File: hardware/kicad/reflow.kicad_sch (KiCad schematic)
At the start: 0 parts

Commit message: hardware: place all schematic components
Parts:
- added A1: ESP32-DevKitV1, reflow:ESP32_DevKitV1_2x15_P2.54_W22.86, symbol reflow:ESP32_DevKitV1
- added C1: 100uF, Capacitor_THT:CP_Radial_D8.0mm_P3.50mm, symbol Device:C
- added C2: 1000uF, Capacitor_THT:CP_Radial_D10.0mm_P5.00mm, symbol Device:C
- added C3, C5, C6, C7, C8: 100nF, Capacitor_THT:C_Disc_D5.0mm_W2.5mm_P2.50mm, symbol Device:C
- added C4: 10uF, Capacitor_THT:CP_Radial_D5.0mm_P2.50mm, symbol Device:C
- added D1: STATUS, LED_THT:LED_D5.0mm, symbol Device:LED
- added D2: 1N5817, Diode_THT:D_DO-41_SOD81_P10.16mm_Horizontal, symbol Device:D_Schottky
- added D3: SMBJ26A, Diode_THT:D_DO-201AD_P15.24mm_Horizontal, symbol Device:D_TVS
- added F1: 15A, Fuse:Fuseholder_Cylinder-5x20mm_Schurter_FAB_0031.8201_Horizontal_Closed, symbol Device:Fuse
- added J1: 24V_IN, TerminalBlock:TerminalBlock_bornier-2_P5.08mm, symbol TerminalBlock:TerminalBlock_bornier-2_P5.08mm
- added J2: HEATER, TerminalBlock:TerminalBlock_bornier-2_P5.08mm, symbol TerminalBlock:TerminalBlock_bornier-2_P5.08mm
- added J3: MAX31855, reflow:Header_1x05_P2.54, symbol reflow:MAX31855_Module
- added J4: OLED, reflow:Header_1x04_P2.54, symbol reflow:OLED_SSD1306_I2C
- added L1: 100uH, Inductor_THT:L_Toroid_Vertical_L20.0mm_D7.0mm_P10.16mm, symbol Device:L
- added Q1: IRFS4710, energy_system:TO-220-3_Vertical_LaserPads_GDS, symbol Transistor_FET:Q_NMOS_GDS
- added Q2, Q3: BS170, Package_TO_SOT_THT:TO-92_Inline, symbol Transistor_FET:Q_NMOS_GDS
- added R1, R2: 1k, Resistor_THT:R_Axial_DIN0207_L6.3mm_D2.5mm_P7.62mm_Horizontal, symbol Device:R
- added R10, R11, R12, R3, R5, R9: 10k, Resistor_THT:R_Axial_DIN0207_L6.3mm_D2.5mm_P7.62mm_Horizontal, symbol Device:R
- added R4: 100, Resistor_THT:R_Axial_DIN0207_L6.3mm_D2.5mm_P7.62mm_Horizontal, symbol Device:R
- added R6: 330, Resistor_THT:R_Axial_DIN0207_L6.3mm_D2.5mm_P7.62mm_Horizontal, symbol Device:R
- added R7, R8: 4.7k, Resistor_THT:R_Axial_DIN0207_L6.3mm_D2.5mm_P7.62mm_Horizontal, symbol Device:R
- added SW1: ENC, Rotary_Encoder:RotaryEncoder_Alps_EC11E-Switch, symbol Device:RotaryEncoder_Switch
- added SW2: START, Button_Switch_THT:SW_PUSH_6mm, symbol Switch:SW_Push
- added U2: LM2576-5.0, energy_system:TO-220-3_Vertical_LaserPads, symbol Regulator_Switching:LM2576T-5
- added U3: LM7812, energy_system:TO-220-3_Vertical_LaserPads, symbol Regulator_Linear:LM7812_TO220

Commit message: hardware: fix MOSFET lib_id to Device:Q_NMOS_GDS; add U2 footprint TODO
Change Q1/Q2/Q3 lib_id from Transistor_FET:Q_NMOS_GDS to Device:Q_NMOS_GDS
(standard KiCad 10 location) in both the PIN_IDS map and COMPONENTS list.
Add inline TODO on U2 noting the 5-pin LM2576 needs a TO-220-5 laser-pad
footprint variant before board layout.

Regenerated reflow.kicad_sch: 37 components, placement check MISSING [],
kicad-cli export exits 0 with no unresolved-symbol warnings,
Transistor_FET:Q_NMOS_GDS count=0, Device:Q_NMOS_GDS count=3.
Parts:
- removed Q1: IRFS4710, energy_system:TO-220-3_Vertical_LaserPads_GDS, symbol Transistor_FET:Q_NMOS_GDS
- removed Q2, Q3: BS170, Package_TO_SOT_THT:TO-92_Inline, symbol Transistor_FET:Q_NMOS_GDS
- added Q1: IRFS4710, energy_system:TO-220-3_Vertical_LaserPads_GDS, symbol Device:Q_NMOS_GDS
- added Q2, Q3: BS170, Package_TO_SOT_THT:TO-92_Inline, symbol Device:Q_NMOS_GDS
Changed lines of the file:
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@@
 	)
 	(symbol
-		(lib_id "Transistor_FET:Q_NMOS_GDS")
+		(lib_id "Device:Q_NMOS_GDS")
 		(at 330 220 0)
 		(unit 1)
@@
 	)
 	(symbol
-		(lib_id "Transistor_FET:Q_NMOS_GDS")
+		(lib_id "Device:Q_NMOS_GDS")
 		(at 270 230 0)
 		(unit 1)
@@
 	)
 	(symbol
-		(lib_id "Transistor_FET:Q_NMOS_GDS")
+		(lib_id "Device:Q_NMOS_GDS")
 		(at 300 230 0)
 		(unit 1)

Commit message: hardware: wire 24V input protection, LM2576 5V, LM7812 12V rails
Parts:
- removed J1: 24V_IN, TerminalBlock:TerminalBlock_bornier-2_P5.08mm, symbol TerminalBlock:TerminalBlock_bornier-2_P5.08mm
- removed J2: HEATER, TerminalBlock:TerminalBlock_bornier-2_P5.08mm, symbol TerminalBlock:TerminalBlock_bornier-2_P5.08mm
- removed Q1: IRFS4710, energy_system:TO-220-3_Vertical_LaserPads_GDS, symbol Device:Q_NMOS_GDS
- removed Q2, Q3: BS170, Package_TO_SOT_THT:TO-92_Inline, symbol Device:Q_NMOS_GDS
- added J1: 24V_IN, TerminalBlock:TerminalBlock_bornier-2_P5.08mm, symbol Connector:Screw_Terminal_01x02
- added J2: HEATER, TerminalBlock:TerminalBlock_bornier-2_P5.08mm, symbol Connector:Screw_Terminal_01x02
- added Q1: IRFS4710, energy_system:TO-220-3_Vertical_LaserPads_GDS, symbol Transistor_FET:Q_NMOS_GDS
- added Q2, Q3: BS170, Package_TO_SOT_THT:TO-92_Inline, symbol Transistor_FET:Q_NMOS_GDS
- C3: value 100nF -> 330nF
- C4: value 10uF -> 100nF; footprint Capacitor_THT:CP_Radial_D5.0mm_P2.50mm -> Capacitor_THT:C_Disc_D5.0mm_W2.5mm_P2.50mm
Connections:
- new net: F1.1, J1.1 (Pin_1)
- new net +12V: C4.1, U3.3 (VO)
- new net +24V: C1.1, C3.1, D3.1 (A1), F1.2, J2.1 (Pin_1), U2.1 (VIN), U3.1 (VI)
- new net +5V: C2.1, L1.2, U2.4 (FB)
- new net GND: C1.2, C2.2, C3.2, C4.2, D2.2 (A), D3.2 (A2), J1.2 (Pin_2), U2.3 (GND), U2.5 (~{ON}/OFF), U3.2 (GND)
- new net SW_OUT: D2.1 (K), L1.1, U2.2 (OUT)

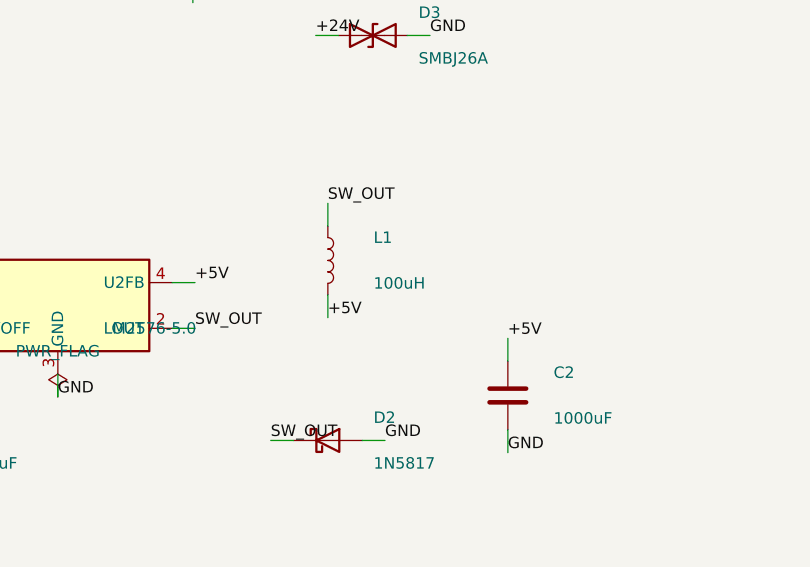
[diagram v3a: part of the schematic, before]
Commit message: hw(buck): swap L1 to 120uH 1A to clear peak-current margin
The 100uH/0.66A shop inductor was below the calculated LM2576 peak
inductor current (~0.82-0.88A at 0.5A load). Replace with the DTU
shop 120uH/1A part: 1A rating exceeds the 0.82A peak with ~20% margin
and reduces ripple from ~0.76A(pp) to ~0.63A(pp).

Update electrical-calcs.md with recomputed ripple (0.63A pp) and peak
(0.82A) for L=120uH, and confirm 1A rating provides adequate margin.
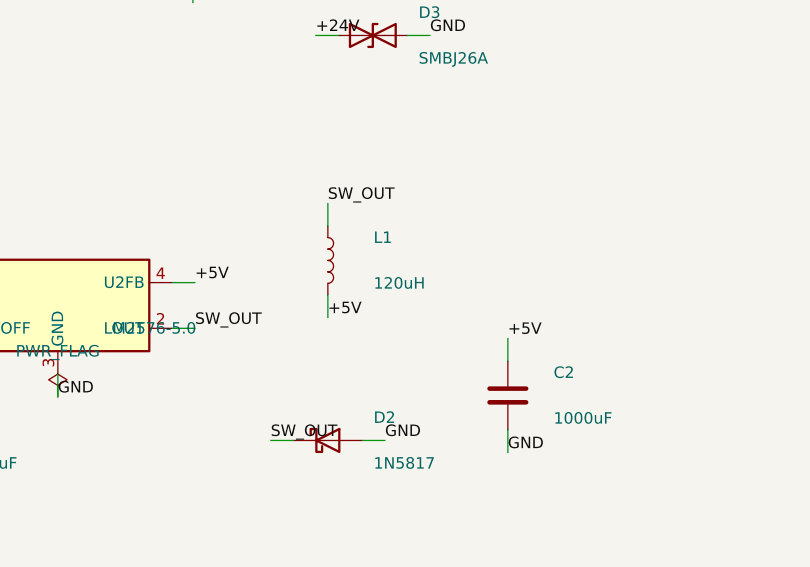
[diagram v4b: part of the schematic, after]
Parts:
- L1: value 100uH -> 120uH
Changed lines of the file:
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@@
 			)
 		)
-		(property "Value" "100uH"
+		(property "Value" "120uH"
 			(at 75.08 77.54 0)
 			(effects

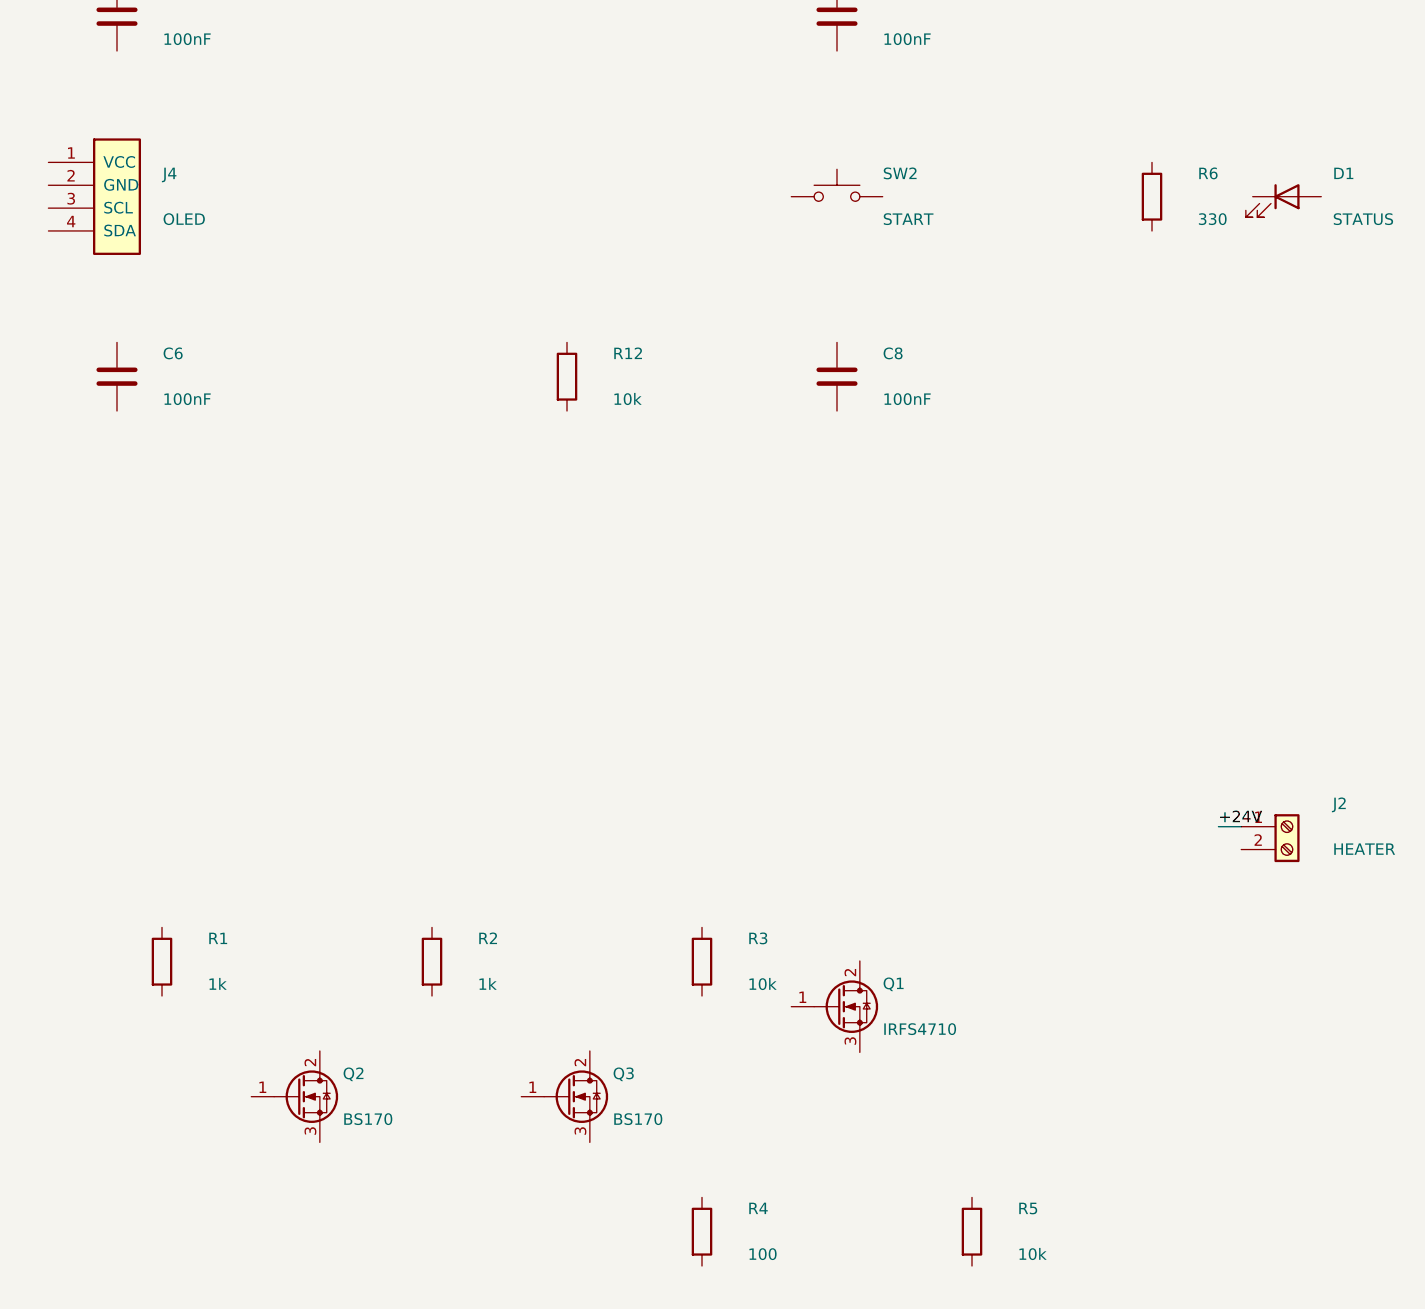
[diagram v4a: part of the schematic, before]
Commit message: hardware: wire IRFS4710 power stage with boot-safe two-stage gate drive
Add NETS_POWERSTAGE wiring pass: two-stage non-inverting BS170 level
shifter (Q2/Q3) driving the IRFS4710 (Q1) low-side heater switch.

- R1 100k Q2.G->GND pulldown, R2 1k HEATER_PWM->Q2.G series
- R3 10k GD_NODE1->+12V pull-up, R4 10k GATE_MAIN->+12V pull-up
- R5 100R series gate resistor, R6 10k Q1.G->GND gate-source pulldown
- HEATER_RET = J2.2 = Q1.D; D4 SMBJ33A TVS clamps drain transients
- Reassign R6 to the gate pulldown (per brief); status-LED resistor -> R13

Boot-safe: floating/low GPIO -> Q2 off -> GD_NODE1=+12V -> Q3 on ->
GATE_MAIN=0V -> Q1 off (heater inherently OFF). Add check_gate_boot_safe.py
asserting the non-inverting pattern and rejecting the single-inverting one.
Power-stage ERC clean; remaining ERC errors are Task-6 refs only.
Append Q1 conduction loss, gate-switching, Vgs and TVS calcs.
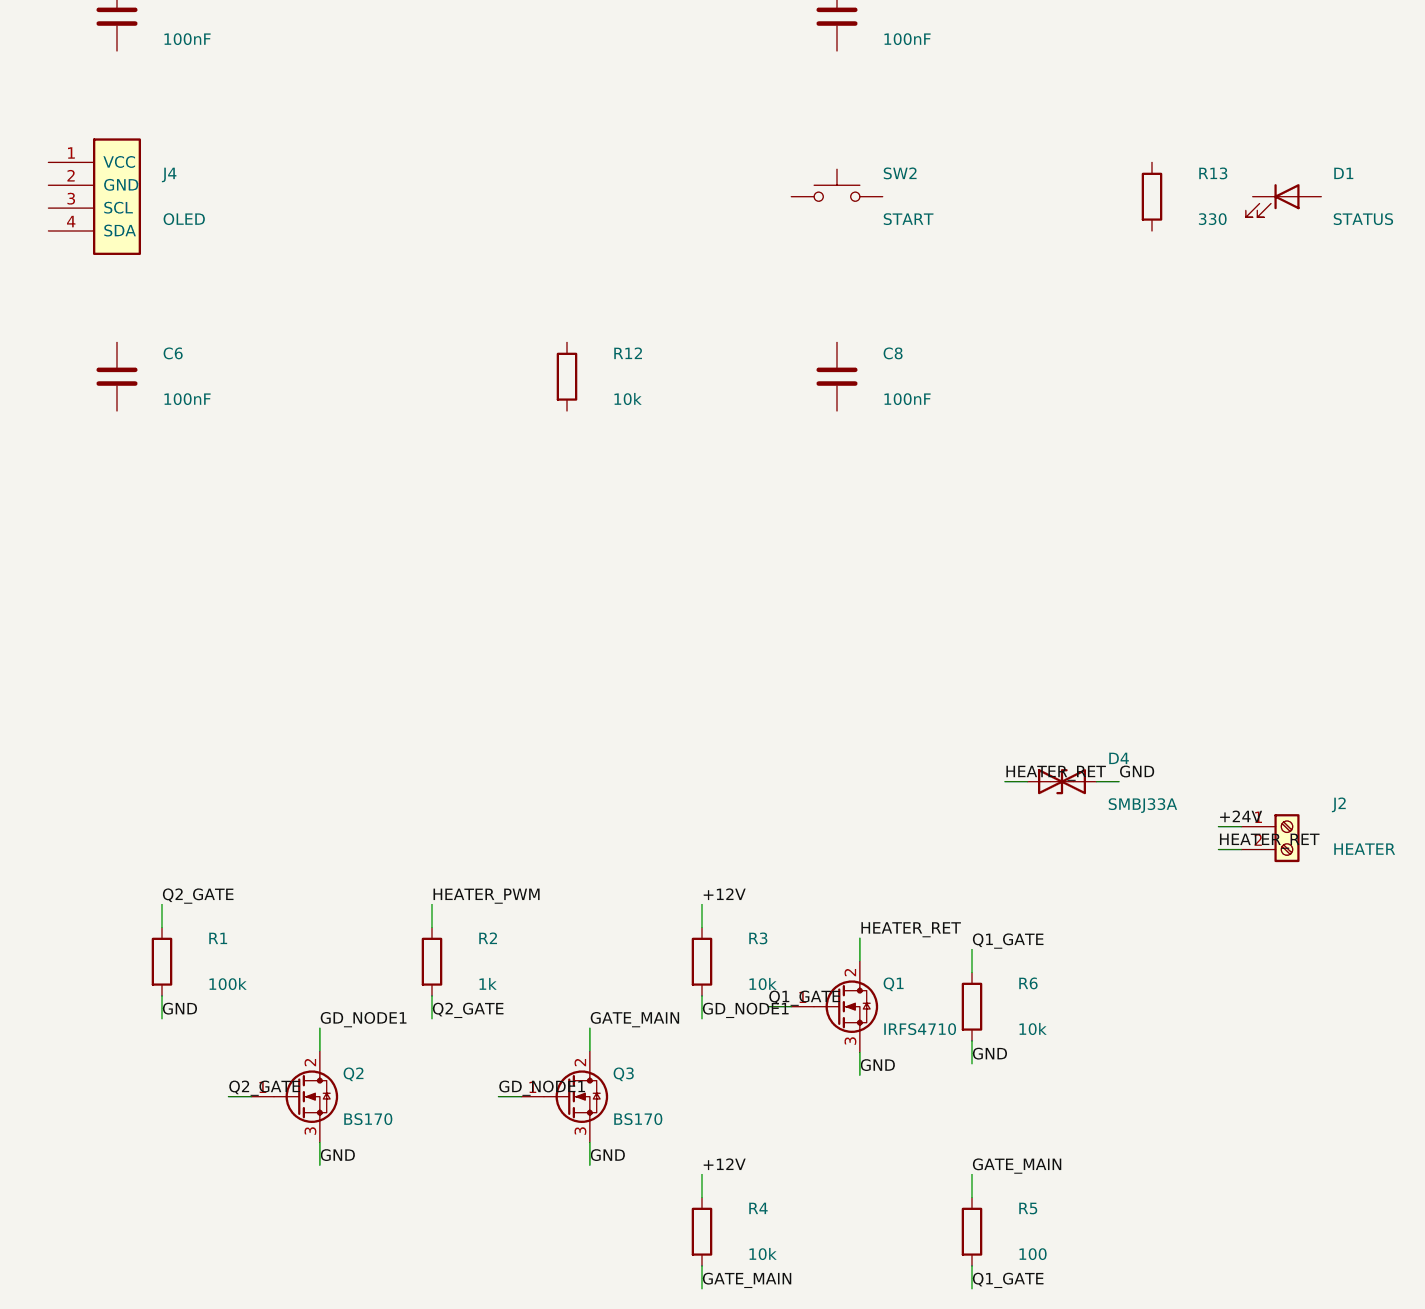
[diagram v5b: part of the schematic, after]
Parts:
- added D4: SMBJ33A, Diode_THT:D_DO-201AD_P15.24mm_Horizontal, symbol Device:D_TVS
- added R13: 330, Resistor_THT:R_Axial_DIN0207_L6.3mm_D2.5mm_P7.62mm_Horizontal, symbol Device:R
- R1: value 1k -> 100k
- R4: value 100 -> 10k
- R5: value 10k -> 100
- R6: value 330 -> 10k
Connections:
- net +12V: now also R3.1, R4.1
- net GND: now also Q1.3 (S), Q2.3 (S), Q3.3 (S), R1.2, R6.2, D4.2 (A2)
- net GD_NODE1: now reaches R3.2
- net GD_NODE1: now also Q2.2 (D), Q3.1 (G)
- net Q2_GATE: now reaches R1.1
- net Q2_GATE: now also Q2.1 (G), R2.2
- net HEATER_PWM: now reaches R2.1
- net Q1_GATE: now reaches R6.1
- net Q1_GATE: now also Q1.1 (G), R5.2
- net HEATER_RET: now reaches Q1.2 (D)
- net HEATER_RET: now also J2.2 (Pin_2), D4.1 (A1)
- net GATE_MAIN: now reaches R4.2
- net GATE_MAIN: now also Q3.2 (D), R5.1

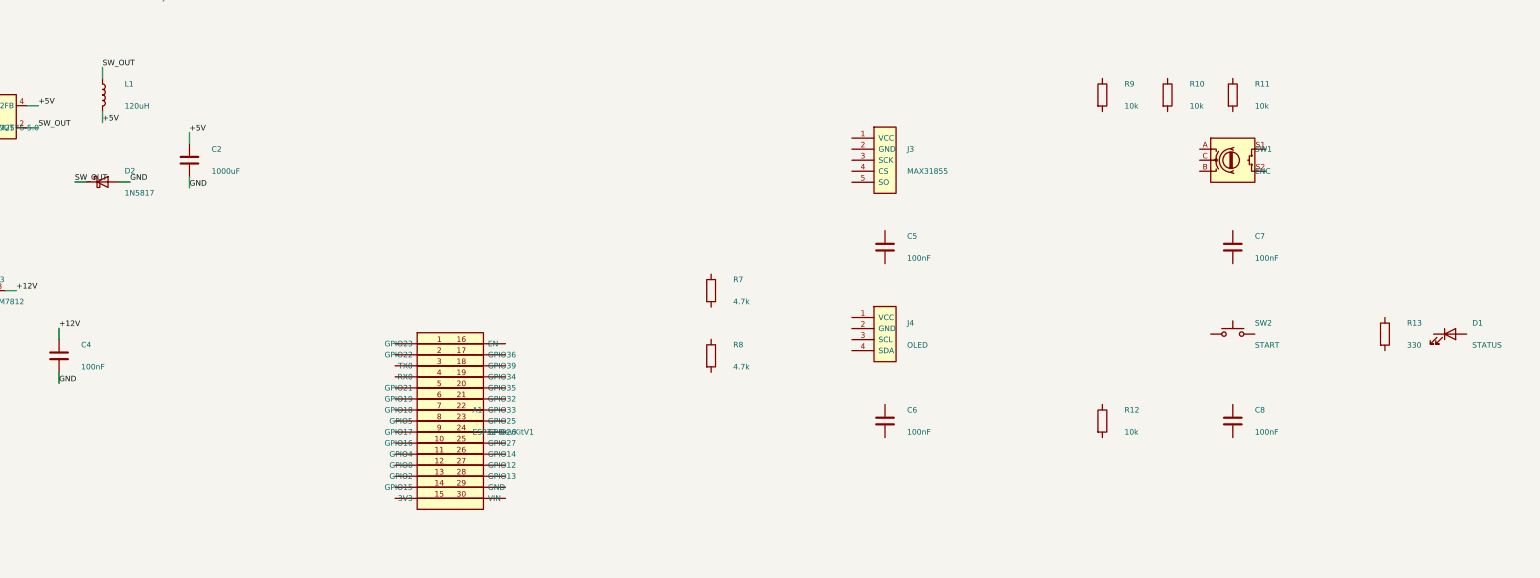
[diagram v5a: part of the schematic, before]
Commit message: hardware: wire ESP32, MAX31855 SPI, OLED I2C, encoder, button, status LED
Add NETS_CTRL pass realising every pinmap GPIO on the ESP32 pins plus the
J3/J4/SW1/SW2/D1 peripherals and their decoupling/debounce caps. Remove the
orphaned R7-R12 placeholders (encoder/button use internal pull-ups; OLED has
its own I2C pull-ups) so the resistor set is R1-R6 + R13. Add +3V3 and +5V
PWR_FLAGs to give those rails an ERC driver. net_contract now passes; the
controller section has no unconnected/undriven ERC errors.
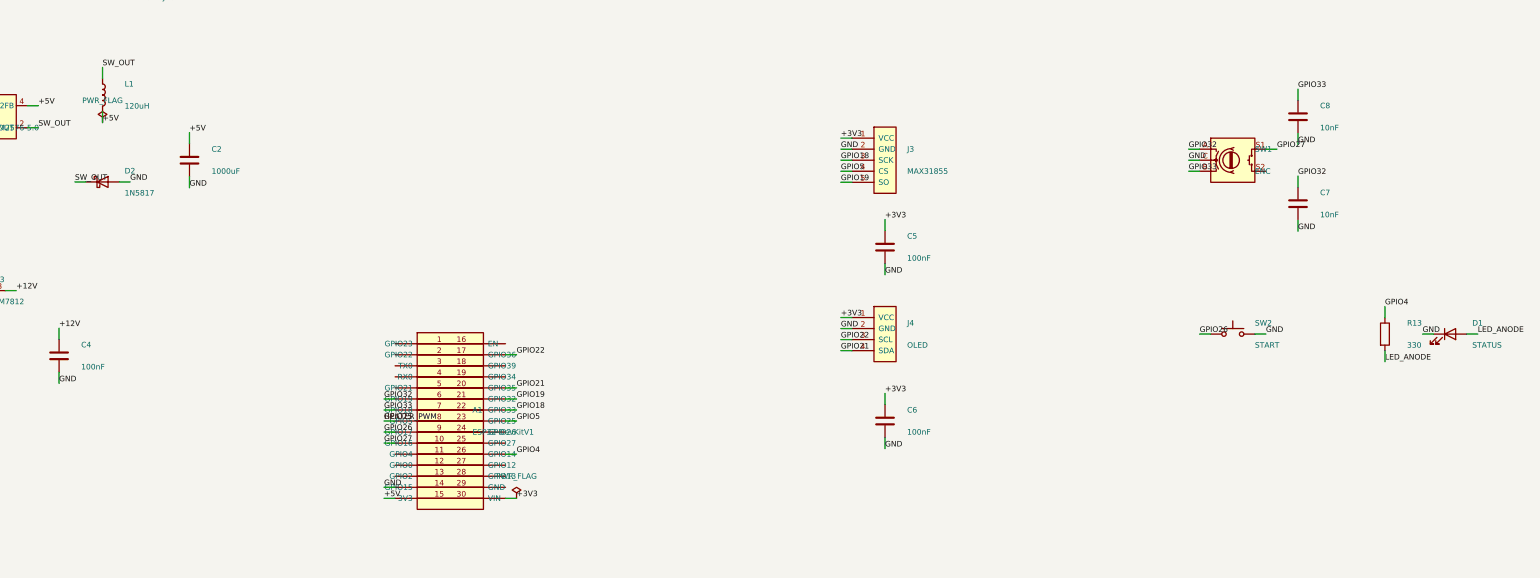
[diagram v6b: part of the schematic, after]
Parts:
- removed R10, R11, R12, R9: 10k, Resistor_THT:R_Axial_DIN0207_L6.3mm_D2.5mm_P7.62mm_Horizontal, symbol Device:R
- removed R7, R8: 4.7k, Resistor_THT:R_Axial_DIN0207_L6.3mm_D2.5mm_P7.62mm_Horizontal, symbol Device:R
- C7, C8: value 100nF -> 10nF
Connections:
- net HEATER_PWM is gone; now on net GPIO25: R2.1
- net +5V: now also A1.15 (VIN)
- net GND: now also A1.14 (GND), C5.2, C6.2, C7.2, C8.2, D1.1 (K), J3.2 (GND), J4.2 (GND), SW1.C, SW2.2
- net +3V3: now reaches J3.1 (VCC)
- net +3V3: now also A1.30 (3V3), C5.1, C6.1, J4.1 (VCC)
- net GPIO18: now reaches J3.3 (SCK)
- net GPIO18: now also A1.22 (GPIO18)
- net GPIO5: now reaches J3.4 (CS)
- net GPIO5: now also A1.23 (GPIO5)
- net GPIO19: now reaches J3.5 (SO)
- net GPIO19: now also A1.21 (GPIO19)
- net GPIO32: now reaches SW1.A
- net GPIO32: now also A1.6 (GPIO32), C7.1
- net GPIO33: now reaches SW1.B
- net GPIO33: now also A1.7 (GPIO33), C8.1
- net GPIO27: now reaches SW1.S1
- net GPIO27: now also A1.10 (GPIO27)
- net GPIO26: now reaches SW2.1
- net GPIO26: now also A1.9 (GPIO26)
- net LED_ANODE: now reaches D1.2 (A)
- net LED_ANODE: now also R13.2
- net GPIO22: now reaches J4.3 (SCL)
- net GPIO22: now also A1.17 (GPIO22)
- net GPIO21: now reaches J4.4 (SDA)
- net GPIO21: now also A1.20 (GPIO21)
- net GPIO4: now reaches A1.26 (GPIO4)
- net GPIO4: now also R13.1
- net GPIO25: now reaches A1.8 (GPIO25)
